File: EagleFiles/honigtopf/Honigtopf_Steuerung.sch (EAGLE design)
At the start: 9 parts

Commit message: corrected currentTemp var and added min and max Temp
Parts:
- added H1, H2: MOUNT-HOLE3.2, holes:MOUNT-HOLE3.2
- R2: value (none) -> 10k
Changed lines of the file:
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@@
 <part name="S1_UP" library="switch-omron" deviceset="10-XX" device=""/>
 <part name="S2_DOWN" library="switch-omron" deviceset="10-XX" device=""/>
-<part name="R2" library="pot" deviceset="TRIM_EU-" device="CA14V"/>
+<part name="R2" library="pot" deviceset="TRIM_EU-" device="CA14V" value="10k"/>
 <part name="DIS1" library="display-lcd" deviceset="TUXGR_16X2_R2" device=""/>
 <part name="R3" library="resistor" deviceset="R-EU_" device="0411/15" value="220"/>
 <part name="JP1_SSR" library="pinhead" deviceset="PINHD-1X2" device=""/>
+<part name="H1" library="holes" deviceset="MOUNT-HOLE" device="3.2"/>
+<part name="H2" library="holes" deviceset="MOUNT-HOLE" device="3.2"/>
 </parts>
 <sheets>
@@
 <instance part="R3" gate="G$1" x="157.48" y="10.16"/>
 <instance part="JP1_SSR" gate="G$1" x="-43.18" y="53.34"/>
+<instance part="H1" gate="G$1" x="10.16" y="106.68"/>
+<instance part="H2" gate="G$1" x="38.1" y="106.68"/>
 </instances>
 <busses>
@@
 <net name="N$15" class="0">
 <segment>
+<pinref part="DIS1" gate="G$1" pin="D7"/>
+<wire x1="162.56" y1="33.02" x2="162.56" y2="50.8" width="0.1524" layer="91"/>
+<wire x1="162.56" y1="33.02" x2="68.58" y2="33.02" width="0.1524" layer="91"/>
+<wire x1="68.58" y1="33.02" x2="68.58" y2="66.04" width="0.1524" layer="91"/>
 <pinref part="PCB1" gate="G$1" pin="D2"/>
-<wire x1="45.72" y1="63.5" x2="45.72" y2="66.04" width="0.1524" layer="91"/>
-<wire x1="45.72" y1="66.04" x2="76.2" y2="66.04" width="0.1524" layer="91"/>
-<wire x1="76.2" y1="66.04" x2="76.2" y2="33.02" width="0.1524" layer="91"/>
-<pinref part="DIS1" gate="G$1" pin="D7"/>
-<wire x1="76.2" y1="33.02" x2="162.56" y2="33.02" width="0.1524" layer="91"/>
-<wire x1="162.56" y1="33.02" x2="162.56" y2="50.8" width="0.1524" layer="91"/>
+<wire x1="68.58" y1="66.04" x2="45.72" y2="66.04" width="0.1524" layer="91"/>
+<wire x1="45.72" y1="66.04" x2="45.72" y2="63.5" width="0.1524" layer="91"/>
 </segment>
 </net>
@@
 </sheet>
 </sheets>
+<errors>
+</errors>
 </schematic>
 </drawing>

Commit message: added supply pins
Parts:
- added JP2_5V_IN: (no value), pinhead:PINHD-1X2
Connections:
- net 5V: now also JP2_5V_IN.1
- net GND: now also JP2_5V_IN.2
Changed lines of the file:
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@@
 <part name="H1" library="holes" deviceset="MOUNT-HOLE" device="3.2"/>
 <part name="H2" library="holes" deviceset="MOUNT-HOLE" device="3.2"/>
+<part name="JP2_5V_IN" library="pinhead" deviceset="PINHD-1X2" device=""/>
 </parts>
 <sheets>
@@
 <instance part="H1" gate="G$1" x="10.16" y="106.68"/>
 <instance part="H2" gate="G$1" x="38.1" y="106.68"/>
+<instance part="JP2_5V_IN" gate="G$1" x="-43.18" y="35.56"/>
 </instances>
 <busses>
@@
 <wire x1="71.12" y1="20.32" x2="71.12" y2="68.58" width="0.1524" layer="91"/>
 <junction x="71.12" y="68.58"/>
-<wire x1="-43.18" y1="53.34" x2="-7.62" y2="53.34" width="0.1524" layer="91"/>
+<wire x1="-43.18" y1="53.34" x2="-35.56" y2="53.34" width="0.1524" layer="91"/>
+<wire x1="-35.56" y1="53.34" x2="-7.62" y2="53.34" width="0.1524" layer="91"/>
 <wire x1="-7.62" y1="53.34" x2="-7.62" y2="-2.54" width="0.1524" layer="91"/>
 <wire x1="-7.62" y1="-2.54" x2="71.12" y2="-2.54" width="0.1524" layer="91"/>
 <wire x1="71.12" y1="-2.54" x2="71.12" y2="20.32" width="0.1524" layer="91"/>
 <junction x="71.12" y="20.32"/>
+<pinref part="JP2_5V_IN" gate="G$1" pin="2"/>
+<wire x1="-45.72" y1="35.56" x2="-35.56" y2="35.56" width="0.1524" layer="91"/>
+<wire x1="-35.56" y1="35.56" x2="-35.56" y2="53.34" width="0.1524" layer="91"/>
+<junction x="-35.56" y="53.34"/>
 </segment>
 </net>
@@
 <wire x1="48.26" y1="17.78" x2="48.26" y2="15.24" width="0.1524" layer="91"/>
 <wire x1="48.26" y1="15.24" x2="-27.94" y2="15.24" width="0.1524" layer="91"/>
-<wire x1="-27.94" y1="15.24" x2="-27.94" y2="91.44" width="0.1524" layer="91"/>
+<wire x1="-27.94" y1="15.24" x2="-27.94" y2="38.1" width="0.1524" layer="91"/>
+<wire x1="-27.94" y1="38.1" x2="-27.94" y2="91.44" width="0.1524" layer="91"/>
 <wire x1="-27.94" y1="91.44" x2="-7.62" y2="91.44" width="0.1524" layer="91"/>
 <wire x1="-7.62" y1="91.44" x2="-7.62" y2="88.9" width="0.1524" layer="91"/>
@@
 <wire x1="48.26" y1="10.16" x2="48.26" y2="15.24" width="0.1524" layer="91"/>
 <junction x="48.26" y="15.24"/>
+<pinref part="JP2_5V_IN" gate="G$1" pin="1"/>
+<wire x1="-45.72" y1="38.1" x2="-27.94" y2="38.1" width="0.1524" layer="91"/>
+<junction x="-27.94" y="38.1"/>
 </segment>
 </net>

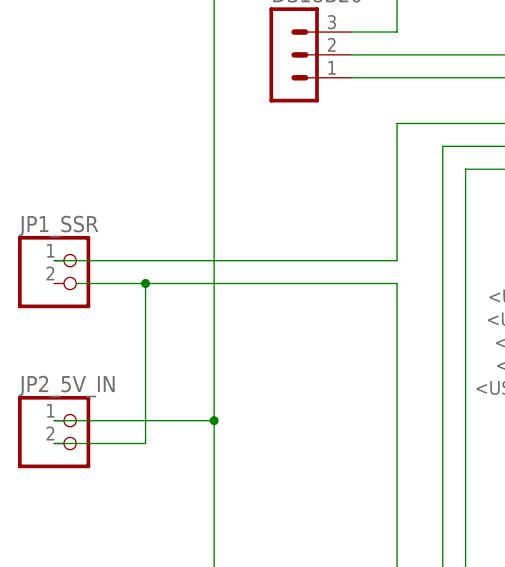
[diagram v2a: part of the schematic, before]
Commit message: changed standard temp to 39
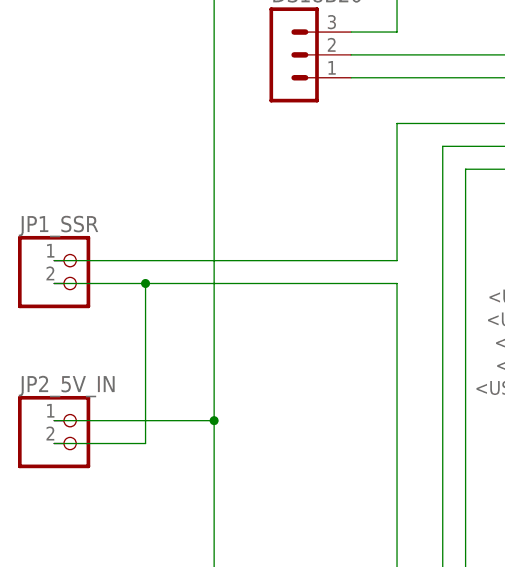
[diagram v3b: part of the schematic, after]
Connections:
- net GND: now also JP1_SSR.2
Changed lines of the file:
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@@
 <wire x1="71.12" y1="20.32" x2="71.12" y2="68.58" width="0.1524" layer="91"/>
 <junction x="71.12" y="68.58"/>
-<wire x1="-43.18" y1="53.34" x2="-35.56" y2="53.34" width="0.1524" layer="91"/>
+<wire x1="-45.72" y1="53.34" x2="-35.56" y2="53.34" width="0.1524" layer="91"/>
 <wire x1="-35.56" y1="53.34" x2="-7.62" y2="53.34" width="0.1524" layer="91"/>
 <wire x1="-7.62" y1="53.34" x2="-7.62" y2="-2.54" width="0.1524" layer="91"/>
@@
 <wire x1="-35.56" y1="35.56" x2="-35.56" y2="53.34" width="0.1524" layer="91"/>
 <junction x="-35.56" y="53.34"/>
+<pinref part="JP1_SSR" gate="G$1" pin="2"/>
 </segment>
 </net>
